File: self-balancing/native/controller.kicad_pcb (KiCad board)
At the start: 6 copper layers, 38 x 38 mm, 151 parts, among them J101 G, J102 5V, J103 T1, J104 R1, J105 G, J106 5V, J107 T2, J108 R2, J109 G, J110 5V, J111 T3, J112 R3, J113 G, J114 5V, J115 T4, J116 R4, J117 G, J118 3V3, J119 SCL, J120 SDA, J121 INT, J122 G, J123 G, J124 3V3, J125 SCK, J126 MISO, J127 MOSI, J128 CS, J129 G, J130 3V3, J131 CAN_RX, J132 CAN_TX, J133 G, J134 OUT1, J135 OUT2, J136 OUT3, J137 OUT4, J138 G, J139 OUT5, J140 OUT6, J141 OUT7, J142 OUT8, J143 G_LINK, J144 5V_LINK, J145 LINK_TX, J146 LINK_RX, J147 RUN, J148 M_OK, J149 G, J150 VTREF, J151 SWDIO, J152 SWCLK, J153 NRST, J154 BOOT, J155 G, J156 3V3, J157 ADC1, J158 ADC2, J159 ADC3, J160 RPM, J161 G, J162 3V3, J163 LED, J164 BUZ, J165 PC8, J166 PC9, J167 PD14, J2 TYPE-C-31-M-12, J3 MOTOR / 6-wire, J4 EXT SPI SENSOR, J5 GPS / UART4, Q1 2N7002, Q2 DMN2310UW-7, U1 STM32H743VIT6, U10 SN74LVC2G17DBVR, U11 W25N01GVZEIG / 128MiB, U12 TLV803EA29DBZR, U13 TPS2116DRLR, U2 TPS62162DSGR / 3.3V, U3 ICM-42688-P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

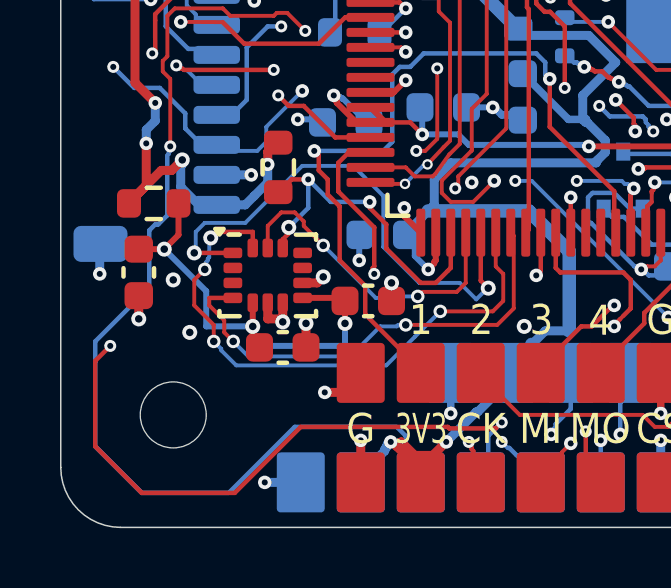
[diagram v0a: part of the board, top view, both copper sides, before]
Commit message: tidy up trace ignore trace center on via
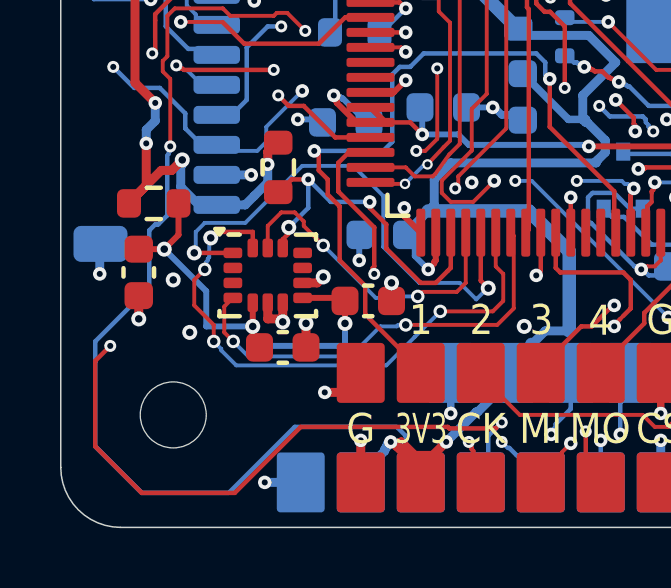
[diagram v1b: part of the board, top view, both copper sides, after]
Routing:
- net IMU_INT: track 15.4 -> 14.5 mm
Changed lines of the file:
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@@
 		(capping no)
 		(filling no)
+		(zone_defaults)
 		(aux_axis_origin 0 38)
 		(pcbplotparams
@@
 	)
 	(segment
-		(start 4.95 30.6)
-		(end 4.95 30.35)
-		(width 0.13)
-		(layer "F.Cu")
-		(net "IMU_INT")
-	)
-	(segment
 		(start 5.45 31.5)
 		(end 5.75 31.8)
@@
 	)
 	(segment
-		(start 5.45 31.1)
-		(end 4.95 30.6)
-		(width 0.13)
-		(layer "F.Cu")
-		(net "IMU_INT")
-	)
-	(segment
 		(start 15.1 28.275)
 		(end 15.1 30.7)
@@
 	)
 	(segment
-		(start 5.7375 30.35)
-		(end 4.95 30.35)
-		(width 0.15)
+		(start 5.45 31.5)
+		(end 5.45 30.6375)
+		(width 0.13)
 		(layer "F.Cu")
 		(net "IMU_INT")
 	)
 	(segment
-		(start 5.45 31.1)
-		(end 5.45 31.5)
+		(start 5.45 30.6375)
+		(end 5.7375 30.35)
 		(width 0.13)
 		(layer "F.Cu")
